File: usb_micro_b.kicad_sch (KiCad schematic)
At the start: 9 parts, among them J1201 USB_C_Receptacle_USB2.0_16P, Q1201 MMBT3904, U1201 PSM712-LF-T7

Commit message: fixed like a bunch of things, power and new xcvr and lights and other goodies, also started layout
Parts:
- removed J1201: USB_C_Receptacle_USB2.0_16P, Connector_USB:USB_C_Receptacle_Amphenol_124019772112A, symbol Connector:USB_C_Receptacle_USB2.0_16P
- removed R1204, R1205: 5.1k, Resistor_SMD:R_0402_1005Metric_Pad0.72x0.64mm_HandSolder, symbol bfr_resistors:RMCF0402FT5K10
- added J1701: MicroUSB, Connector_USB:USB_Micro-B_Amphenol_10118194-0001LF_Horizontal, symbol bfr_connectors:USB_B_Micro
- added R1704: 100k, Resistor_SMD:R_0402_1005Metric_Pad0.72x0.64mm_HandSolder, symbol bfr_resistors:RMCF0402FT100K
- renumbered D1201 to D1701, Q1201 to Q1701, R1201 to R1701, R1202 to R1702, R1203 to R1703, U1201 to U1701
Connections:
- net GND: now also J1701.5 (GND), J1701.6 (Shield), R1704.1
- net USB_D+: now also U1701.1, J1701.3 (D+); no longer U1701.2
- net USB_D-: now also U1701.2, J1701.2 (D-); no longer U1701.1
- net at D1701.2 (A): now also J1701.1 (VBUS)
- new net: J1701.4 (ID), R1704.2
- no-connect marks 2 -> 0
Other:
- moved on the sheet: D1701, Q1701, R1701, R1702, R1703, U1701

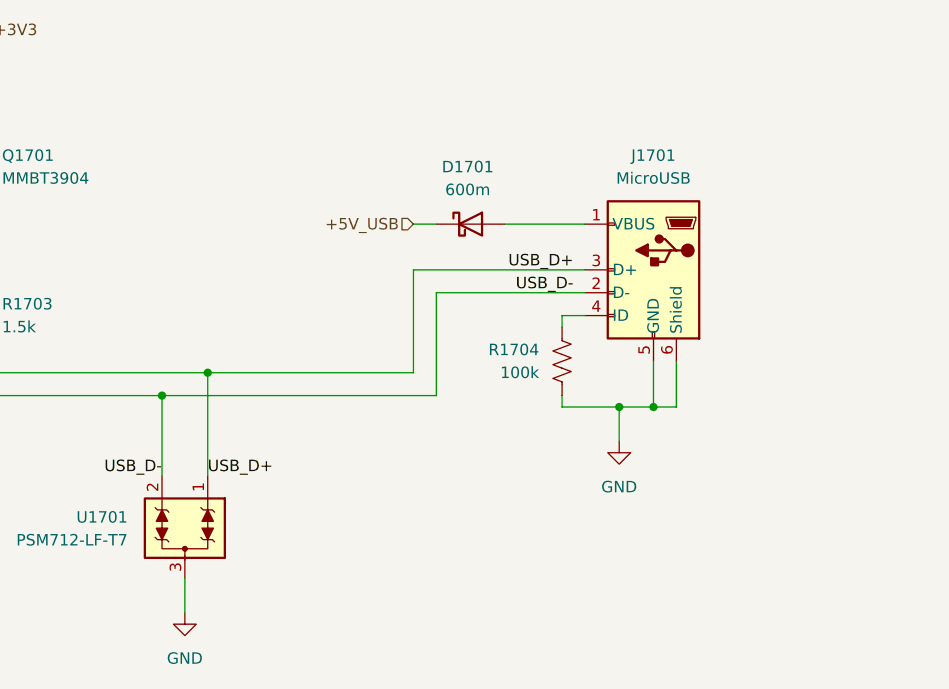
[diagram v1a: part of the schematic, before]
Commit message: quicksave on some R.S. T.S. (mostly layout changes, small pin changes for better routing)
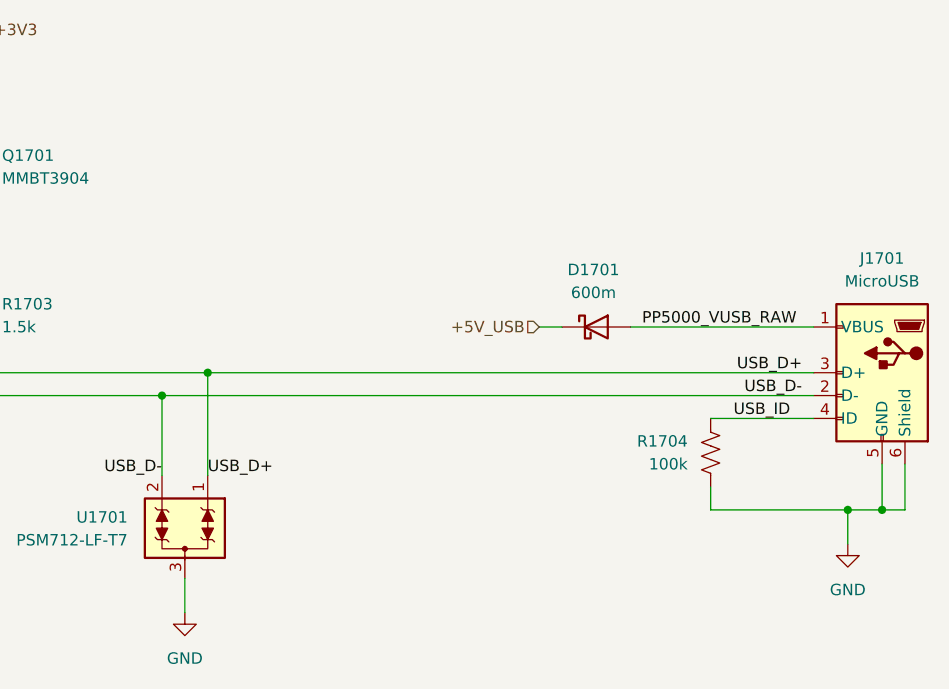
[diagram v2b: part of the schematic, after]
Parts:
- removed J1701: MicroUSB, Connector_USB:USB_Micro-B_Amphenol_10118194-0001LF_Horizontal, symbol bfr_connectors:USB_B_Micro
- added J1701: MicroUSB, Connector_USB:USB_Micro-B_Molex-105133-0001, symbol bfr_connectors:USB_B_Micro_Vertical
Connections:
- net GND: now also J1701.5 (GND), J1701.6 (Shield)
- net USB_D+: now also J1701.3 (D+)
- net USB_D-: now also J1701.2 (D-)
- net USB_ID: now reaches R1704.2
- net USB_ID: now also J1701.4 (ID)
- net PP5000_VUSB_RAW: now reaches D1701.2 (A)
- net PP5000_VUSB_RAW: now also J1701.1 (VBUS)
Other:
- moved on the sheet: D1701, R1704
